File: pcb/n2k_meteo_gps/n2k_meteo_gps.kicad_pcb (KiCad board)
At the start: 2 copper layers, 55 x 54.5 mm, 33 parts, among them J10 3.3-5V, U1 LM7805_TO220, U3 MCP2562-E-P, U4 PC817, U5 ESP32-C3_SUPERMINI, U6 PC817

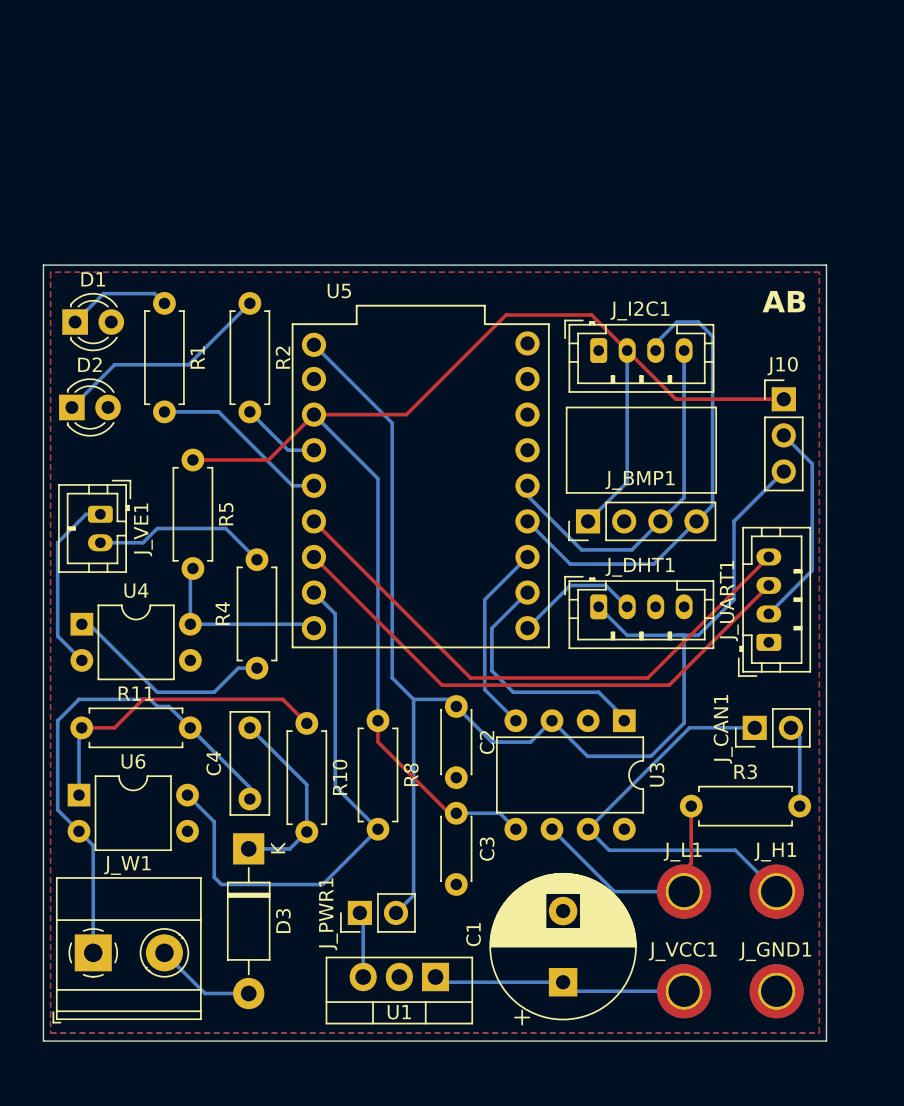
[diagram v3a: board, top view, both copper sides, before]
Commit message: - Added support for esp32-s3-zero - Added support for 3 leds (pwr, gps fix, & n2k) - Enhancements to NMEA parser x UART GPS - Experimental support for SoftwareSerial - Minor enhancements
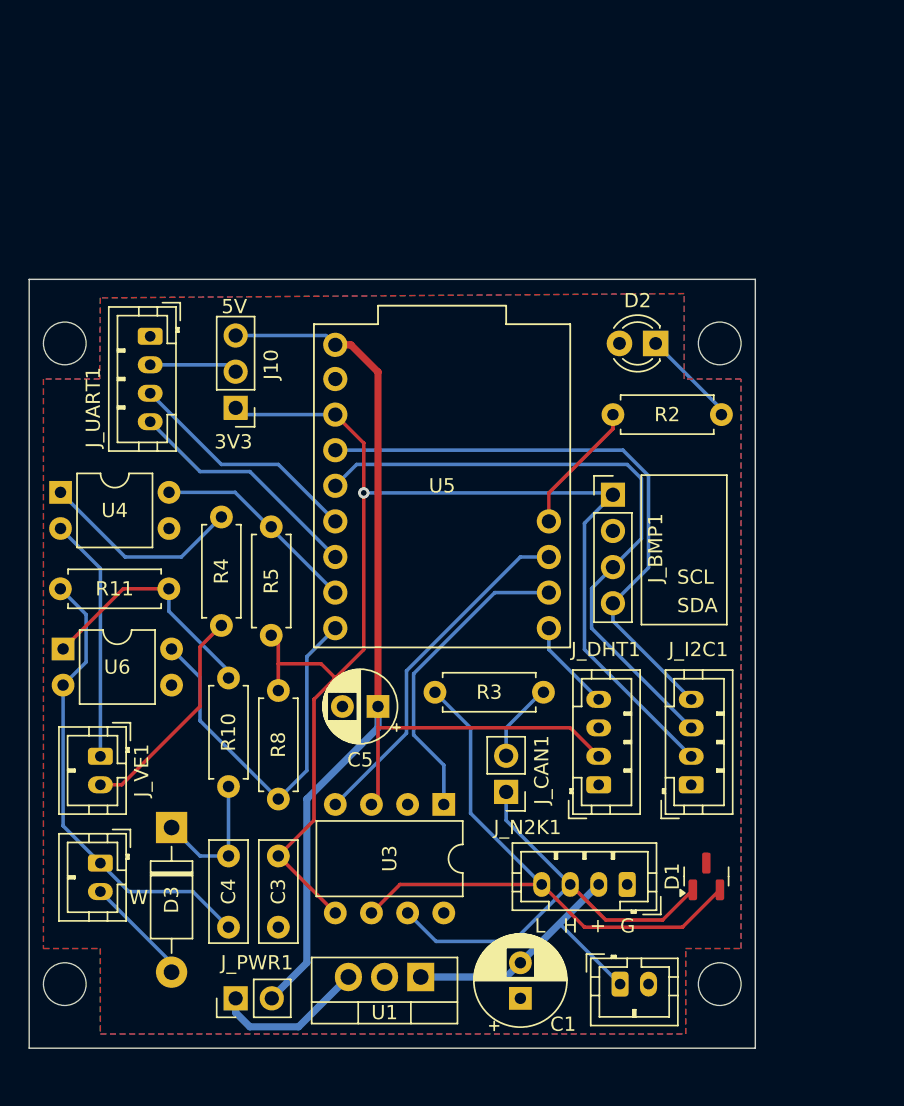
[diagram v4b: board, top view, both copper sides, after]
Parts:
- removed C2: 100nF, Capacitor_THT:C_Disc_D4.3mm_W1.9mm_P5.00mm
- removed J_GND1: CAN GND, MountingHole:MountingHole_2.2mm_M2_DIN965_Pad_TopBottom
- removed J_H1: CAN H, MountingHole:MountingHole_2.2mm_M2_DIN965_Pad_TopBottom
- removed J_L1: CAN L, MountingHole:MountingHole_2.2mm_M2_DIN965_Pad_TopBottom
- removed J_VCC1: CAN 12V, MountingHole:MountingHole_2.2mm_M2_DIN965_Pad_TopBottom
- removed R1: 100Ω, Resistor_THT:R_Axial_DIN0207_L6.3mm_D2.5mm_P7.62mm_Horizontal
- added C5: 220uF, Capacitor_THT:CP_Radial_D5.0mm_P2.50mm, F.Cu at (42.5, 71.8)
- added J_12_PWR1: 12V Led, Connector_JST:JST_PH_B2B-PH-K_1x02_P2.00mm_Vertical, F.Cu at (59.5, 91.2)
- added J_N2K1: J_N2K, Connector_JST:JST_PH_B4B-PH-K_1x04_P2.00mm_Vertical, F.Cu at (60.0, 84.2)
- C1: value 100uF -> 220uF; footprint Capacitor_THT:CP_Radial_D10.0mm_P5.00mm -> Capacitor_THT:CP_Radial_D6.3mm_P2.50mm
- C3: footprint Capacitor_THT:C_Disc_D4.3mm_W1.9mm_P5.00mm -> Capacitor_THT:C_Disc_D7.0mm_W2.5mm_P5.00mm
- D1: value LED -> SM712_SOT23; footprint LED_THT:LED_D3.0mm -> Package_TO_SOT_SMD:SOT-23
- J_W1: value Engine RPM Input -> Engine RPM; footprint TerminalBlock_Phoenix:TerminalBlock_Phoenix_MKDS-1,5-2_1x02_P5.00mm_Horizontal -> Connector_JST:JST_PH_B2B-PH-K_1x02_P2.00mm_Vertical
- R5: value 4.7KΩ -> 2.2KΩ
- R8: value 4.7K -> 2.2K
- U5: footprint Library:WAVESHARE_DEVKIT_ESP32-C3-ZERO -> Library:WAVESHARE_DEVKIT_ESP32-C3-ZERO-ALT
- moved D1 59.0 mm to (65.6, 83.7), turned to 90 degrees
- moved J_UART1 48.5 mm to (26.6, 45.8), turned to -90 degrees
- moved D2 41.2 mm to (62.0, 46.2), turned to 180 degrees
- moved J10 38.5 mm to (32.5, 50.8), turned to 180 degrees
- moved J_I2C1 31.2 mm to (64.5, 77.2), turned to 90 degrees
- moved R2 26.7 mm to (59.0, 51.2), turned to 0 degrees
- moved R3 19.7 mm to (46.5, 70.8)
- moved J_CAN1 18.0 mm to (51.5, 77.8), turned to 180 degrees
- moved J_VE1 17.0 mm to (23.1, 75.2)
- moved U3 14.0 mm to (47.2, 78.6)
- moved R5 13.5 mm to (35.0, 66.8), turned to 90 degrees
- moved C3 12.9 mm to (35.5, 82.2)
- moved J_DHT1 12.5 mm to (58.0, 77.2), turned to 90 degrees
- moved R11 11.5 mm to (27.9, 63.5), turned to 180 degrees
- moved R4 10.9 mm to (31.6, 58.4), turned to -90 degrees
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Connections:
- C1 pad 1: +12V -> GND
- C1 pad 2: GND -> +12V
- D1 pad 1: Net-(D1-K) -> Net-(D1-A1)
- D1 pad 2: GND -> Net-(D1-A2)
- J_CAN1 pad 1: Net-(J_CAN1-Pin_1) -> Net-(D1-A1)
- J_DHT1 pad 1: +5V -> GND
- J_DHT1 pad 2: Net-(J_DHT1-Pin_2) -> +5V
- J_DHT1 pad 4: GND -> Net-(J_DHT1-Pin_4)
- J_I2C1 pad 3: Net-(J_BMP1-Pin_4) -> Net-(J_BMP1-Pin_3)
- J_I2C1 pad 4: Net-(J_BMP1-Pin_3) -> Net-(J_BMP1-Pin_4)
- R2 pad 1: Net-(D2-K) -> Net-(U5-GPIO9)
- R2 pad 2: Net-(U5-GPIO0) -> Net-(D2-K)
- R3 pad 1: Net-(J_L1-Pin_1) -> Net-(D1-A2)
- R5 pad 2: Net-(U5-GPIO5) -> Net-(U5-GPIO4)
- R8 pad 2: Net-(U5-GPIO4) -> Net-(U5-GPIO5)
- U3 pad 6: Net-(J_L1-Pin_1) -> Net-(D1-A2)
- U3 pad 7: Net-(J_CAN1-Pin_1) -> Net-(D1-A1)
- U4 pad 4: Net-(U5-GPIO5) -> Net-(U5-GPIO4)
- U5 pad 0: Net-(U5-GPIO0) -> Net-(J_BMP1-Pin_4)
- U5 pad 1: Net-(U5-GPIO1) -> Net-(J_BMP1-Pin_3)
- U5 pad 2: Net-(J_UART1-Pin_4) -> Net-(J_UART1-Pin_3)
- U5 pad 3: Net-(J_UART1-Pin_3) -> Net-(J_UART1-Pin_4)
- U5 pad 6: Net-(J_DHT1-Pin_2) -> Net-(J_DHT1-Pin_4)
- U5 pad 9: Net-(J_BMP1-Pin_4) -> Net-(U5-GPIO9)
- U6 pad 4: Net-(U5-GPIO4) -> Net-(U5-GPIO5)
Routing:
- net Net-(D1-A2): track 0.00 -> 44.2 mm
- net Net-(D1-A1): track 0.00 -> 32.8 mm
- net Net-(J_CAN1-Pin_1): track 29.7 -> 0.00 mm
- net Net-(U5-GPIO4): track 38.4 -> 14.6 mm
- net Net-(J_UART1-Pin_4): track 40.0 -> 16.9 mm
- net Net-(J_UART1-Pin_3): track 38.6 -> 16.7 mm
- net Net-(J_BMP1-Pin_3): track 25.1 -> 44.4 mm
- net Net-(J_L1-Pin_1): track 17.3 -> 0.00 mm
- net Net-(U5-GPIO5): track 12.8 -> 27.3 mm
- net +5V: track 94.7 -> 81.5 mm
- net Net-(U5-GPIO1): track 12.6 -> 0.00 mm
- net Net-(U3-RXD): track 13.6 -> 24.8 mm
- net Net-(U5-GPIO9): track 0.00 -> 9.36 mm
- net Net-(J_DHT1-Pin_2): track 8.86 -> 0.00 mm
- net Net-(D2-K): track 15.5 -> 6.91 mm
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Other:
- board size 55 x 54.5 mm -> 51 x 54 mm
- board text added: "+"
- board text added: "3V3"
- board text added: "5V"
- board text added: "G"
- board text added: "H"
- board text added: "L"
- board text added: "SCL"
- board text added: "SDA"
- board text added: "W"
- board text removed: "AB"

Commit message: stuff...
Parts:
- removed U1: LM7805_TO220, Package_TO_SOT_THT:TO-220-3_Vertical
- added U2: TSR_1-2450, Converter_DCDC:Converter_DCDC_TRACO_TSR-1_THT, F.Cu at (47.0, 89.2)
- C1: value 220uF -> 10uF; footprint Capacitor_THT:CP_Radial_D6.3mm_P2.50mm -> Capacitor_THT:C_Disc_D7.0mm_W2.5mm_P5.00mm
- C5: value 220uF -> 22uF; footprint Capacitor_THT:CP_Radial_D5.0mm_P2.50mm -> Capacitor_THT:C_Disc_D7.0mm_W2.5mm_P5.00mm
- moved R10 9.12 mm to (35.4, 78.2), turned to 180 degrees
- moved R8 3.65 mm to (35.0, 74.2), turned to 180 degrees
- moved C1 2.24 mm to (53.5, 94.2)
- moved U3 2.18 mm to (47.2, 76.5)
- moved D3 1.92 mm to (28.1, 82.2)
- moved C5 1.00 mm to (42.5, 70.8)
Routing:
- net Net-(R10-Pad1): track 17.2 -> 32.2 mm
- net +3.3V: track 95.5 -> 90.5 mm
- net Net-(U5-GPIO5): track 27.3 -> 23.1 mm
- net Net-(U3-TXD): track 21.9 -> 19.7 mm
- net Net-(U3-RXD): track 24.8 -> 22.6 mm
- net Net-(J_PWR1-Pin_1): track 10.8 -> 12.9 mm
- net Net-(D3-A): track 7.73 -> 9.65 mm
- net Net-(D3-K): track 9.71 -> 8.08 mm
- net +5V: track 81.5 -> 79.9 mm
- net Net-(J_VE1-Pin_2): track 15.6 -> 17.1 mm
- net Net-(J_BMP1-Pin_4): track 41.8 -> 42.8 mm
- net Net-(D1-A1): track 32.8 -> 31.9 mm

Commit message: PCB
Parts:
- moved D1 13.1 mm to (52.6, 82.2), turned to 180 degrees
- moved J_N2K1 5.50 mm to (65.5, 84.3)
- moved R4 3.29 mm to (32.0, 61.7)
- moved D2 3.06 mm to (59.3, 45.0), turned to 0 degrees
- moved C1 2.06 mm to (54.0, 92.2)
- moved J_SPARE1 2.06 mm to (28.6, 45.2)
- moved J10 1.58 mm to (34.0, 50.3)
- moved U2 1.12 mm to (47.5, 88.2)
- moved C3 0.71 mm to (36.0, 81.8)
- moved C4 0.71 mm to (32.5, 86.8)
- moved C5 0.71 mm to (43.0, 70.2)
- moved D3 0.71 mm to (28.6, 81.7)
- moved J_12_PWR1 0.71 mm to (60.0, 90.8)
- moved J_BMP1 0.71 mm to (59.5, 56.4)
- moved J_CAN1 0.71 mm to (52.0, 77.2)
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- renumbered J_UART1 to J_SPARE1
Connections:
- D2 pad 1: Net-(D2-K) -> GND
- D2 pad 2: GND -> Net-(D2-A)
- J_CAN1 pad 1: Net-(D1-A1) -> Net-(D1-A2)
- R2 pad 2: Net-(D2-K) -> Net-(D2-A)
- R3 pad 1: Net-(D1-A2) -> Net-(D1-A1)
- U3 pad 6: Net-(D1-A2) -> Net-(D1-A1)
- U3 pad 7: Net-(D1-A1) -> Net-(D1-A2)
- U5 pad 0: Net-(J_BMP1-Pin_4) -> unconnected-(U5-GPIO0-Pad0)
- U5 pad 1: Net-(J_BMP1-Pin_3) -> unconnected-(U5-GPIO1-Pad1)
- U5 pad 10: (no net) -> unconnected-(U5-GPIO10-Pad10)
- U5 pad 20: (no net) -> Net-(J_BMP1-Pin_3)
- U5 pad 21: (no net) -> Net-(J_BMP1-Pin_4)
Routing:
- net Net-(D1-A2): track 44.6 -> 20.7 mm
- net Net-(D1-A1): track 31.9 -> 43.0 mm
- net Net-(J_BMP1-Pin_3): track 44.2 -> 33.6 mm
- net Net-(J_BMP1-Pin_4): track 42.8 -> 32.4 mm
- net Net-(D2-A): track 0.00 -> 8.61 mm
- net Net-(D2-K): track 6.91 -> 0.00 mm
- net Net-(R10-Pad1): track 32.2 -> 27.1 mm
- net Net-(J_VE1-Pin_2): track 17.1 -> 13.8 mm
- net Net-(J_SPARE1-Pin_4): track 16.9 -> 15.4 mm
- net Net-(J_SPARE1-Pin_3): track 16.7 -> 15.2 mm
- net Net-(U5-GPIO5): track 23.1 -> 21.7 mm
- net +3.3V: track 90.5 -> 91.7 mm
- net Net-(J_PWR1-Pin_1): track 12.9 -> 11.7 mm
- net Net-(R4-Pad1): track 14.3 -> 13.6 mm
- net +5V: track 79.9 -> 80.5 mm
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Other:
- board size 51 x 54 mm -> 50 x 54 mm
- board text added: "ESP32-C3"
- board text added: "Rx"

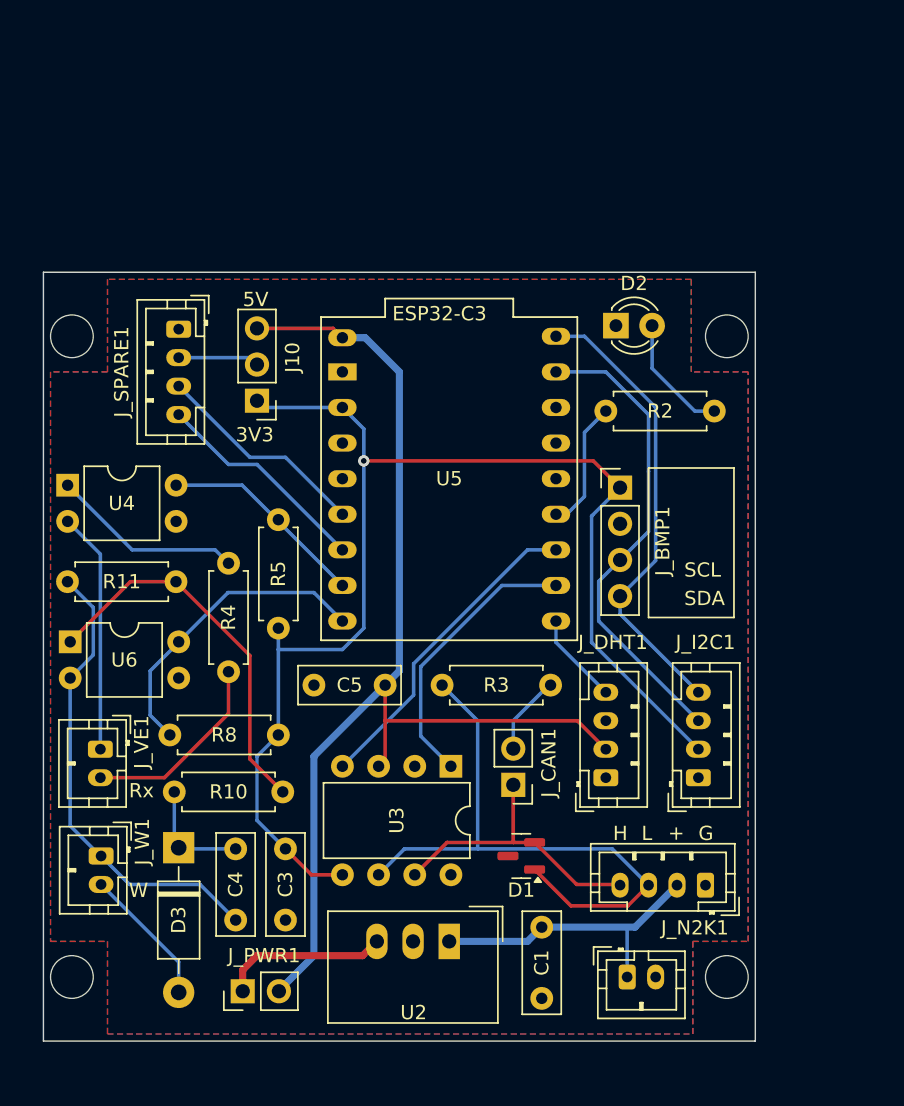
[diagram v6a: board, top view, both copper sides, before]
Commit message: PCB - added xiao seeed studio
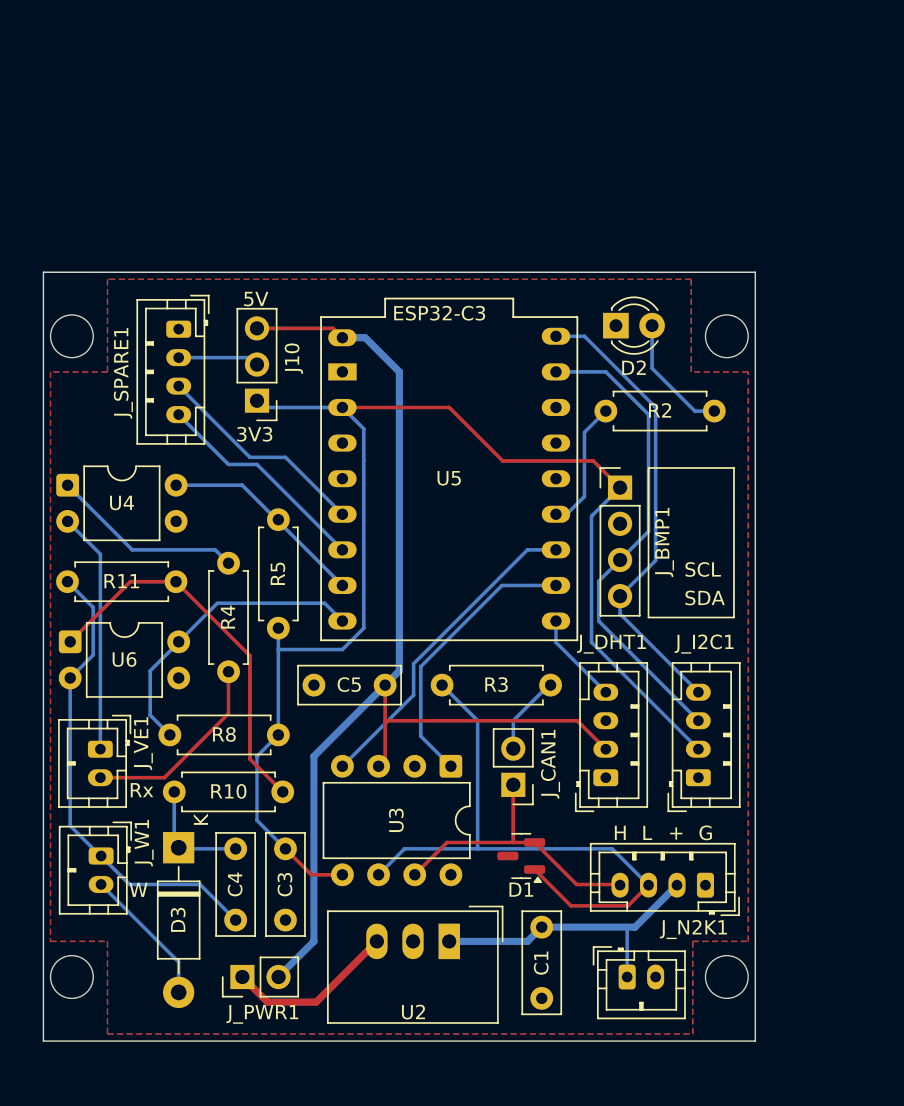
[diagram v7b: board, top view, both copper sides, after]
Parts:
- U5: footprint Library:WAVESHARE_DEVKIT_ESP32-C3-ZERO-ALT -> MyLib:WAVESHARE_DEVKIT_ESP32-C3-ZERO-ALT
- moved J_PWR1 1.00 mm to (33.0, 90.8)
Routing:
- net +3.3V: track 91.7 -> 94.8 mm, vias 1 -> 0
- net +5V: track 80.5 -> 79.5 mm
- net Net-(U5-GPIO5): track 21.7 -> 21.1 mm

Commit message: PCB
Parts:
- removed U4, U6: PC817, Package_DIP:DIP-4_W7.62mm
- added U1: HCPL-2631, Package_DIP:DIP-8_W7.62mm, F.Cu at (24.6, 60.2)
- R5: value 2.2KΩ -> 1KΩ
- R8: value 2.2K -> 1KΩ
- moved R11 7.59 mm to (21.3, 60.2), turned to -90 degrees
- moved R4 6.27 mm to (30.1, 55.8), turned to 180 degrees
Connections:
- R5 pad 1: +3.3V -> Net-(U5-GPIO4)
- R5 pad 2: Net-(U5-GPIO4) -> Net-(U1-VO2)
- R8 pad 1: +3.3V -> Net-(U5-GPIO5)
- R8 pad 2: Net-(U5-GPIO5) -> Net-(U1-VO1)
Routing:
- net Net-(U1-VO1): track 0.00 -> 15.3 mm
- net Net-(U1-VO2): track 0.00 -> 12.4 mm
- net Net-(U5-GPIO5): track 21.1 -> 9.86 mm
- net Net-(J_VE1-Pin_2): track 13.8 -> 23.2 mm
- net Net-(U5-GPIO4): track 14.6 -> 5.74 mm
- net Net-(J_VE1-Pin_1): track 17.0 -> 10.1 mm
- net +3.3V: track 94.8 -> 88.9 mm
- net Net-(U1-A1): track 27.1 -> 25.5 mm
- net Net-(J_W1-Pin_1): track 32.9 -> 34.2 mm
- net Net-(U1-A2): track 13.6 -> 14.4 mm
